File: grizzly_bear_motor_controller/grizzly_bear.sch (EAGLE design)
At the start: 54 parts, among them Q1 PH7030L, Q2 PH7030L, Q3 PH7030L, Q4 PH7030L, Q5 FDD4141TO252, U1 A4940, U2 ATMEGA32U4-AU, U3 ACS714, U4 UA78L00, Y1 16MHz

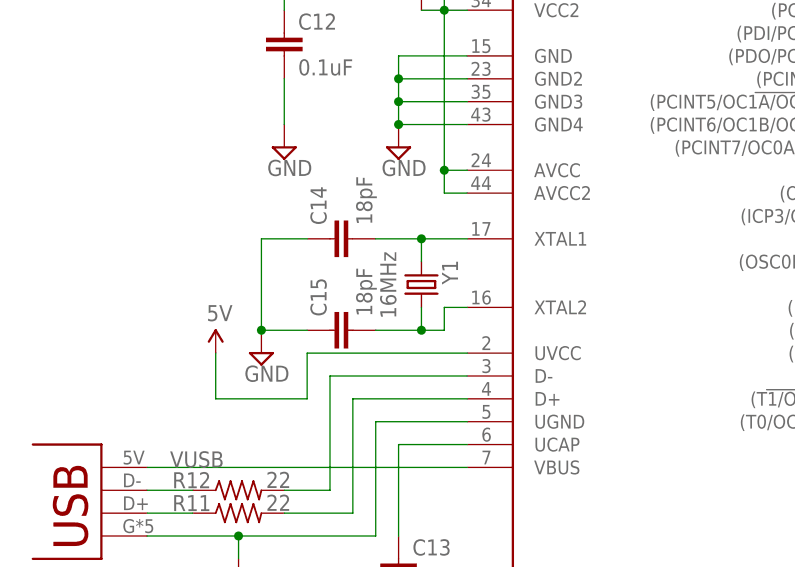
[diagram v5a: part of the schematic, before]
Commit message: Expand drill holes of crystal
Change-Id: Ic247b6292cbf41966bf56fa91863cb11911d346f
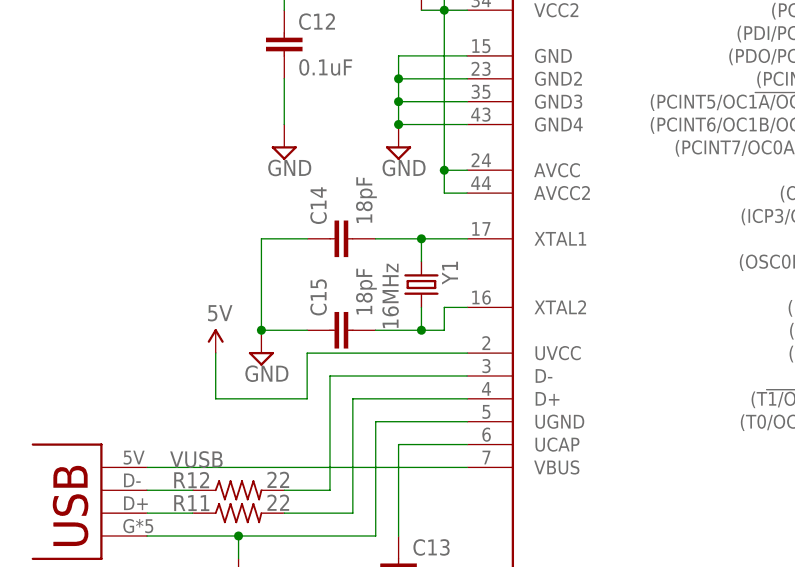
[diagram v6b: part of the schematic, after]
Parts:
- Y1: device SparkFun-FreqCtrl:CRYSTALHC49US -> pie:CRYSTALHC49US
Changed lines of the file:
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@@
 <part name="C14" library="SparkFun-Passives" deviceset="CAP" device="0603-CAP" value="18pF"/>
 <part name="C15" library="SparkFun-Passives" deviceset="CAP" device="0603-CAP" value="18pF"/>
-<part name="Y1" library="SparkFun-FreqCtrl" deviceset="CRYSTAL" device="HC49US" value="16MHz"/>
 <part name="SUPPLY6" library="supply2" deviceset="GND" device=""/>
 <part name="U$6" library="SparkFun-Aesthetics" deviceset="5V" device=""/>
@@
 <part name="U$14" library="SparkFun-Aesthetics" deviceset="5V" device=""/>
 <part name="C100" library="pie" deviceset="CAP_POL" device="G" value="470uF"/>
+<part name="Y1" library="pie" deviceset="CRYSTAL" device="HC49US" value="16MHz"/>
 </parts>
 <sheets>
@@
 <instance part="C14" gate="G$1" x="-81.28" y="55.88" rot="R90"/>
 <instance part="C15" gate="G$1" x="-81.28" y="45.72" rot="R90"/>
-<instance part="Y1" gate="G$1" x="-73.66" y="50.8" smashed="yes" rot="R90">
-<attribute name="NAME" x="-69.596" y="50.8" size="1.778" layer="95" rot="R90"/>
-<attribute name="VALUE" x="-76.454" y="46.99" size="1.778" layer="96" rot="R90"/>
-</instance>
 <instance part="SUPPLY6" gate="GND" x="-91.44" y="43.18"/>
 <instance part="U$6" gate="G$1" x="-73.66" y="81.28"/>
@@
 <instance part="U$14" gate="G$1" x="-25.4" y="127"/>
 <instance part="C100" gate="G$1" x="124.46" y="114.3"/>
+<instance part="Y1" gate="G$1" x="-73.66" y="50.8" smashed="yes" rot="R90">
+<attribute name="NAME" x="-69.596" y="50.8" size="1.778" layer="95" rot="R90"/>
+<attribute name="VALUE" x="-76.2" y="45.72" size="1.778" layer="96" rot="R90"/>
+</instance>
 </instances>
 <busses>
@@
 <pinref part="C14" gate="G$1" pin="2"/>
 <wire x1="-68.58" y1="55.88" x2="-73.66" y2="55.88" width="0.1524" layer="91"/>
-<pinref part="Y1" gate="G$1" pin="2"/>
 <wire x1="-73.66" y1="55.88" x2="-78.74" y2="55.88" width="0.1524" layer="91"/>
-<wire x1="-73.66" y1="53.34" x2="-73.66" y2="55.88" width="0.1524" layer="91"/>
 <junction x="-73.66" y="55.88"/>
 <pinref part="U2" gate="G$1" pin="XTAL1"/>
+<pinref part="Y1" gate="G$1" pin="2"/>
+<wire x1="-73.66" y1="53.34" x2="-73.66" y2="55.88" width="0.1524" layer="91"/>
 </segment>
 </net>
@@
 <pinref part="C15" gate="G$1" pin="2"/>
 <wire x1="-71.12" y1="45.72" x2="-73.66" y2="45.72" width="0.1524" layer="91"/>
-<pinref part="Y1" gate="G$1" pin="1"/>
 <wire x1="-73.66" y1="45.72" x2="-78.74" y2="45.72" width="0.1524" layer="91"/>
-<wire x1="-73.66" y1="48.26" x2="-73.66" y2="45.72" width="0.1524" layer="91"/>
 <junction x="-73.66" y="45.72"/>
 <pinref part="U2" gate="G$1" pin="XTAL2"/>
-</segment>
-</net>
+<pinref part="Y1" gate="G$1" pin="1"/>
+<wire x1="-73.66" y1="48.26" x2="-73.66" y2="45.72" width="0.1524" layer="91"/>
+</segment>
+</net>

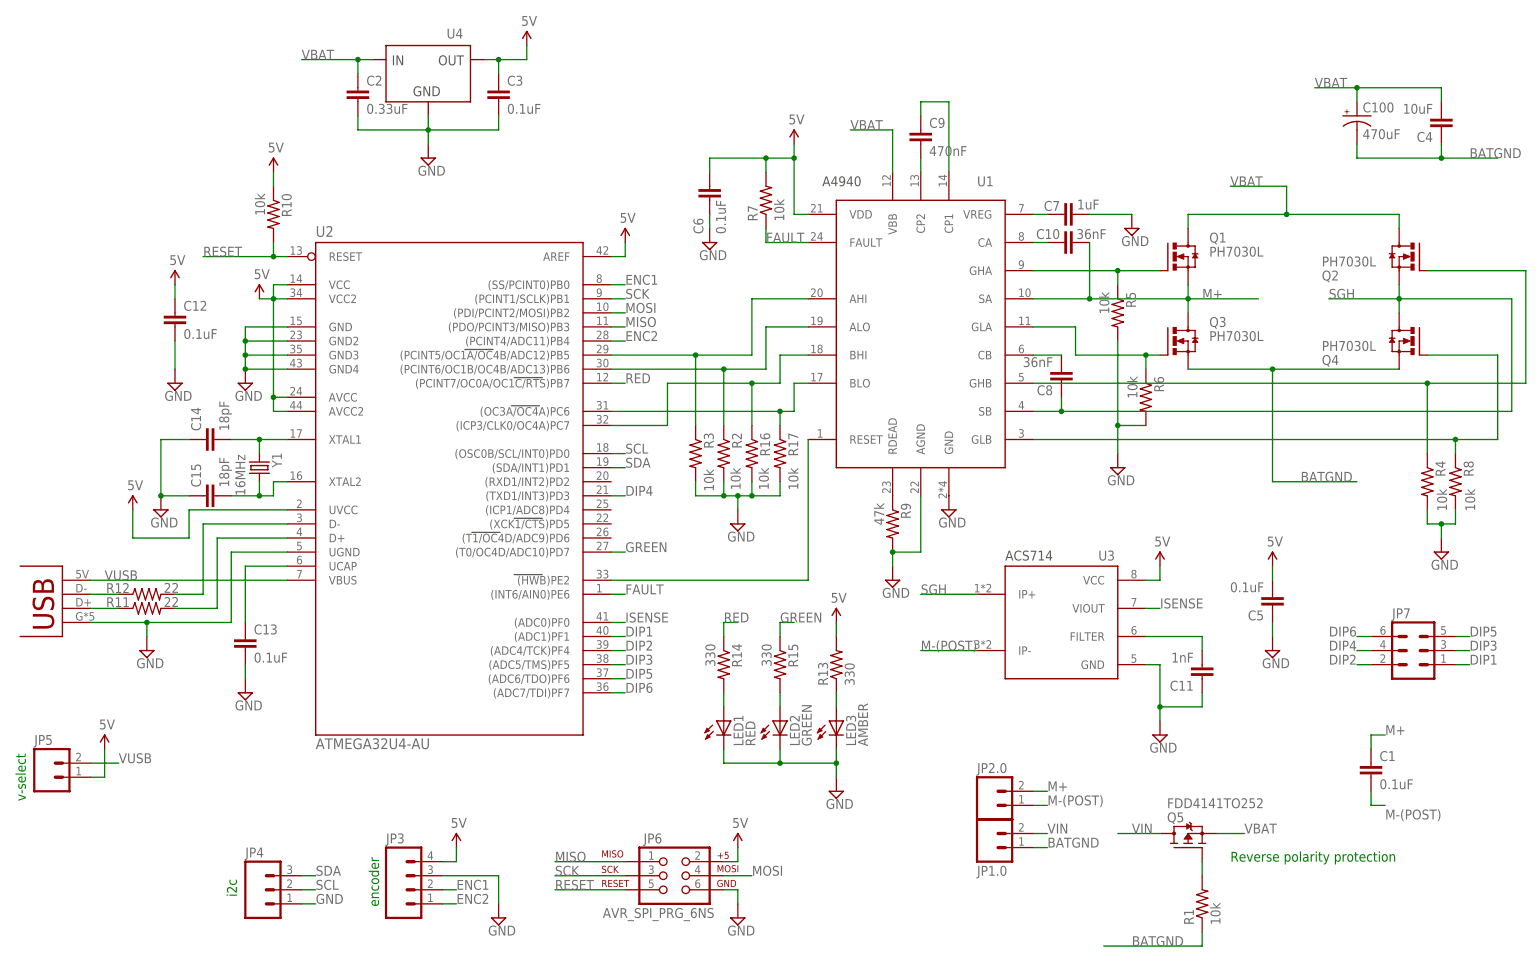
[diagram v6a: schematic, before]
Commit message: Major rearranging of passives and routing cleanup
Change-Id: Ie28f99ff09a130c551b81e80368b51638bbcf09f
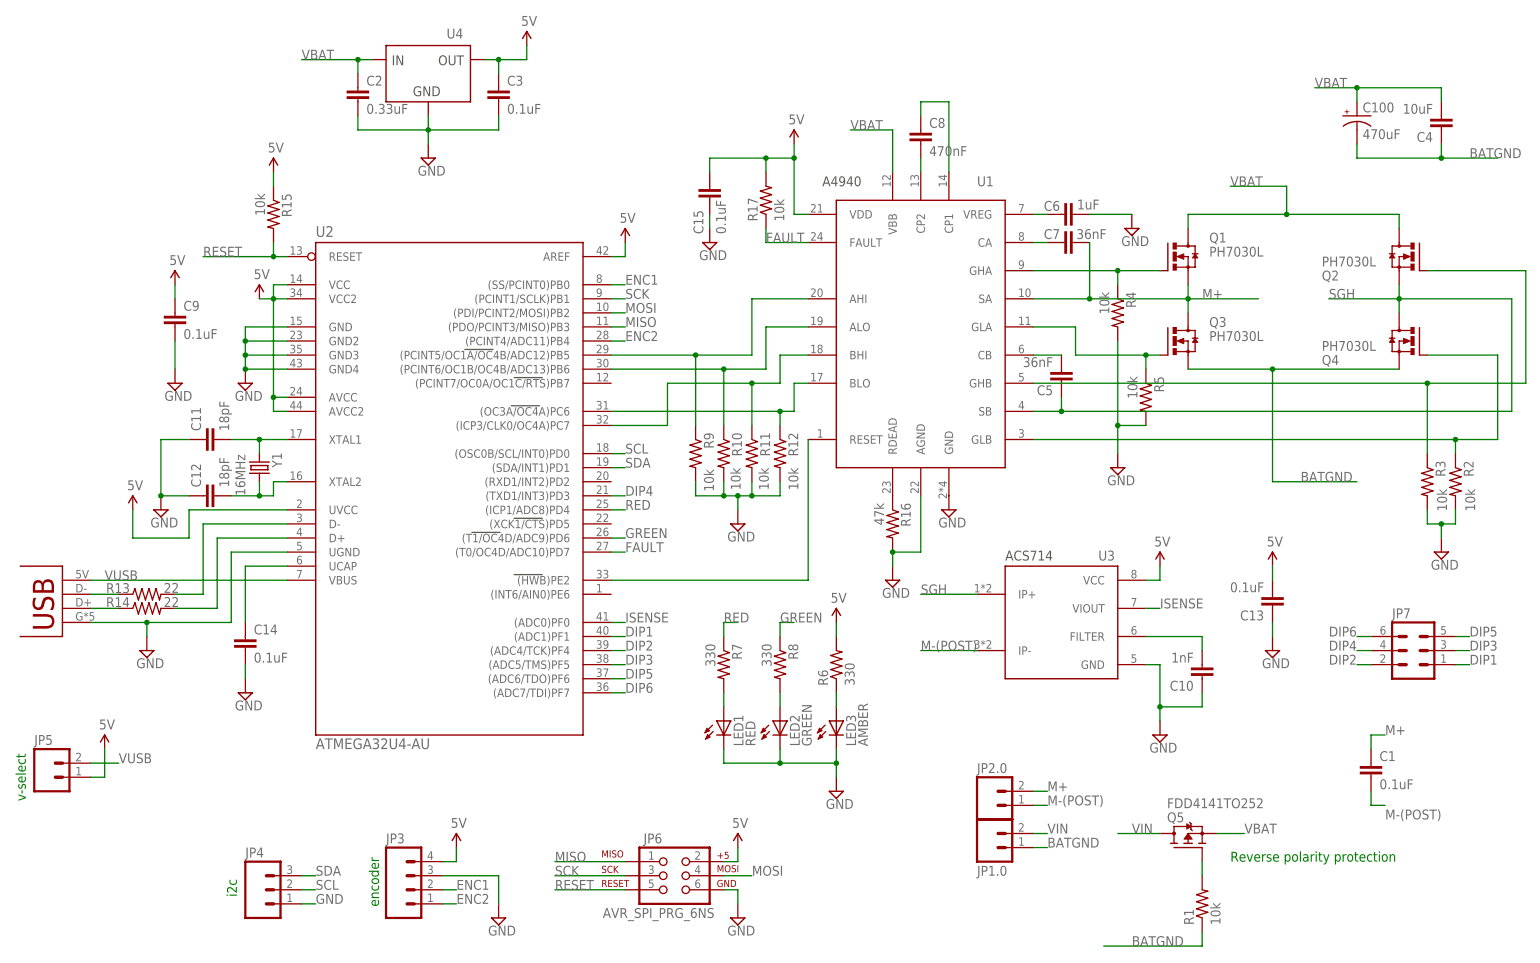
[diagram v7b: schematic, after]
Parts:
- C10: value 36nF -> 1nF
- C11: value 1nF -> 18pF
- C12: value 0.1uF -> 18pF
- C14, C15: value 18pF -> 0.1uF
- C5: value 0.1uF -> 36nF
- C6: value 0.1uF -> 1uF
- C7: value 1uF -> 36nF
- C8: value 36nF -> 470nF
- C9: value 470nF -> 0.1uF
- R10: device rcl:R-US_R0603 -> resistor:R-US_R0603
- R11, R12: value 22 -> 10k; device rcl:R-US_R0603 -> resistor:R-US_R0603
- R13, R14: value 330 -> 22; device resistor:R-US_R0603 -> rcl:R-US_R0603
- R15: value 330 -> 10k; device resistor:R-US_R0603 -> rcl:R-US_R0603
- R16: value 10k -> 47k
- R6, R7, R8: value 10k -> 330
- R9: value 47k -> 10k
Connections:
- net 5V: now also C13.2, C15.1, C9.1, R15.1, R17.2, R6.2; no longer C12.1, C5.2, C6.1, R10.1, R13.2, R7.2
- net AHI: now also R9.1; no longer R3.1
- net FAULT: now also R17.1, U2.(T0/OC4D/ADC10)PD7; no longer R7.1, U2.(INT6/AIN0)PE6
- net GND: now also C10.1, C12.1, C13.1, C14.2, C15.2, C9.2, R10.2, R11.2, R12.2; no longer C12.2, C13.2, C14.1, C15.1, C5.1, C7.2, R17.2, R6.2, R8.2
- net GREEN: now also R8.1, U2.(T1/OC4D/ADC9)PD6; no longer R15.1, U2.(T0/OC4D/ADC10)PD7
- net M+: now also C7.2; no longer C10.2
- net N$11: now also R2.1; no longer R8.1
- net N$13: now also R3.1; no longer R4.1
- net N$14: now also C5.2; no longer C8.2
- net N$16: now also C7.1; no longer C10.1
- net N$17: now also C6.1; no longer C7.1
- net N$18: now also C14.1; no longer C13.1
- net N$19: now also C8.1; no longer C9.1
- net N$2: now also R4.1; no longer R5.1
- net N$20: now also R12.1; no longer R17.1
- net N$21: now also R11.1; no longer R16.1
- net N$22: now also R10.1; no longer R2.1
- net N$23: now also R7.2; no longer R14.2
- net N$24: now also R14.1; no longer R11.1
- net N$25: now also R6.1; no longer R13.1
- net N$26: now also C11.2; no longer C14.2
- net N$27: now also C12.2; no longer C15.2
- net N$28: now also C10.2; no longer C11.2
- net N$29: now also R13.1; no longer R12.1
- net N$3: now also C8.2; no longer C9.2
- net N$5: now also R8.2; no longer R15.2
- net N$6: now also R16.1; no longer R9.1
- net N$7: now also R13.2; no longer R12.2
- net N$8: now also R5.1; no longer R6.1
- net N$9: now also R14.2; no longer R11.2
- net RED: now also R7.1, U2.(ICP1/ADC8)PD4; no longer R14.1, U2.(PCINT7/OC0A/OC1C/RTS)PB7
- net RESET: now also R15.2; no longer R10.2
- net SGH: now also C5.1; no longer C8.1
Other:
- moved on the sheet: C10, C11, C12, C13, C14, C15, C5, C6, C7, C8, C9, R10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
